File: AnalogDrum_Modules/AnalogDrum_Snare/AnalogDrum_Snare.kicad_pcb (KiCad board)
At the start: 2 copper layers, 100.3 x 160 mm, 143 parts, among them J101 Conn_01x05_Male, Q201 2N3904, Q202 2N3904, Q501 2N3904, Q502 2N3904, Q503 2N3904, SW601 SW_DPDT_x2, SW602 SW_DPDT_x2, U201 NE5532, U301 NE5532, U302 NE5532, U401 LM13700, U402 NE5532, U501 TL074, U502 LM358, U601 TL074, U701 NE5532

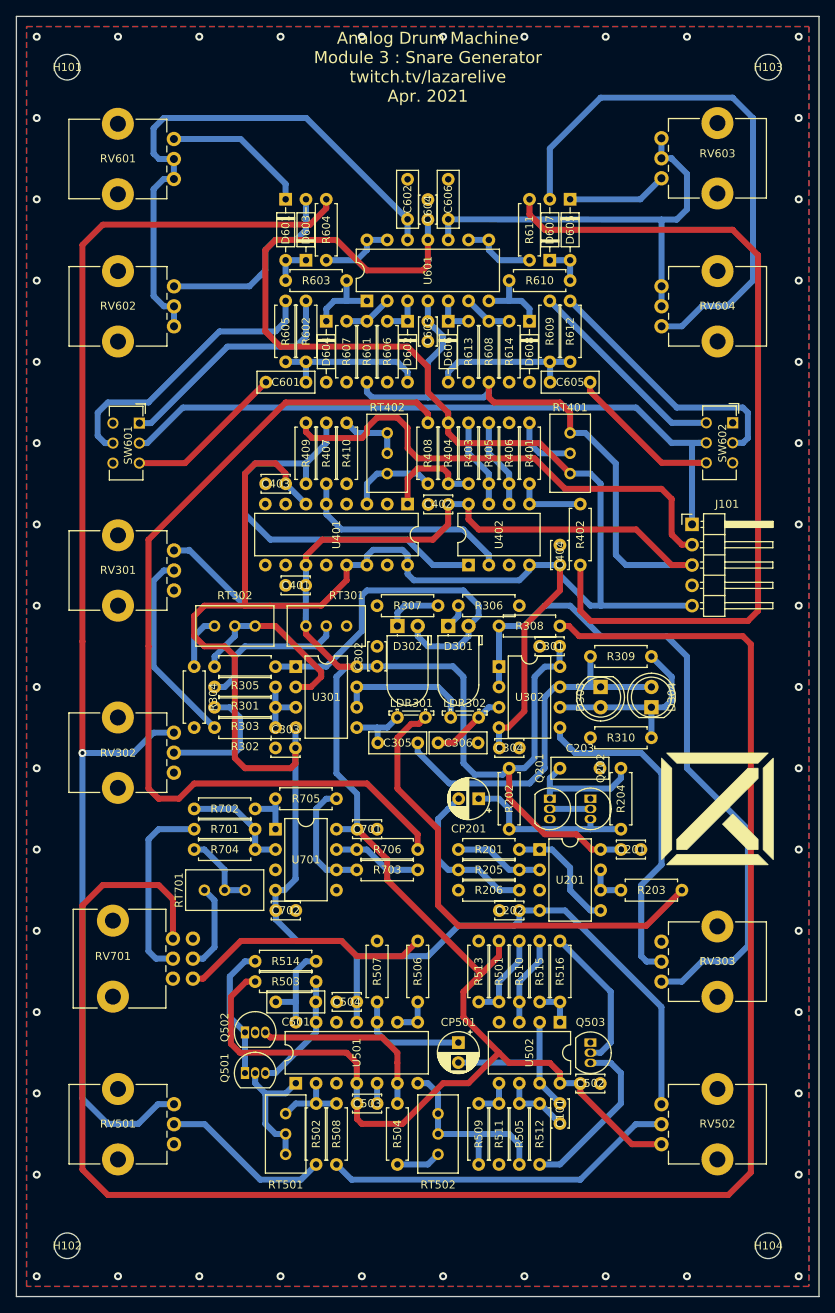
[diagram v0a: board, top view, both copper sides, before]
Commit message: Version 0.1.1
Corrections mineures :
- Vérification des potentiomètres
- Passage des connecteurs de carte e n JST
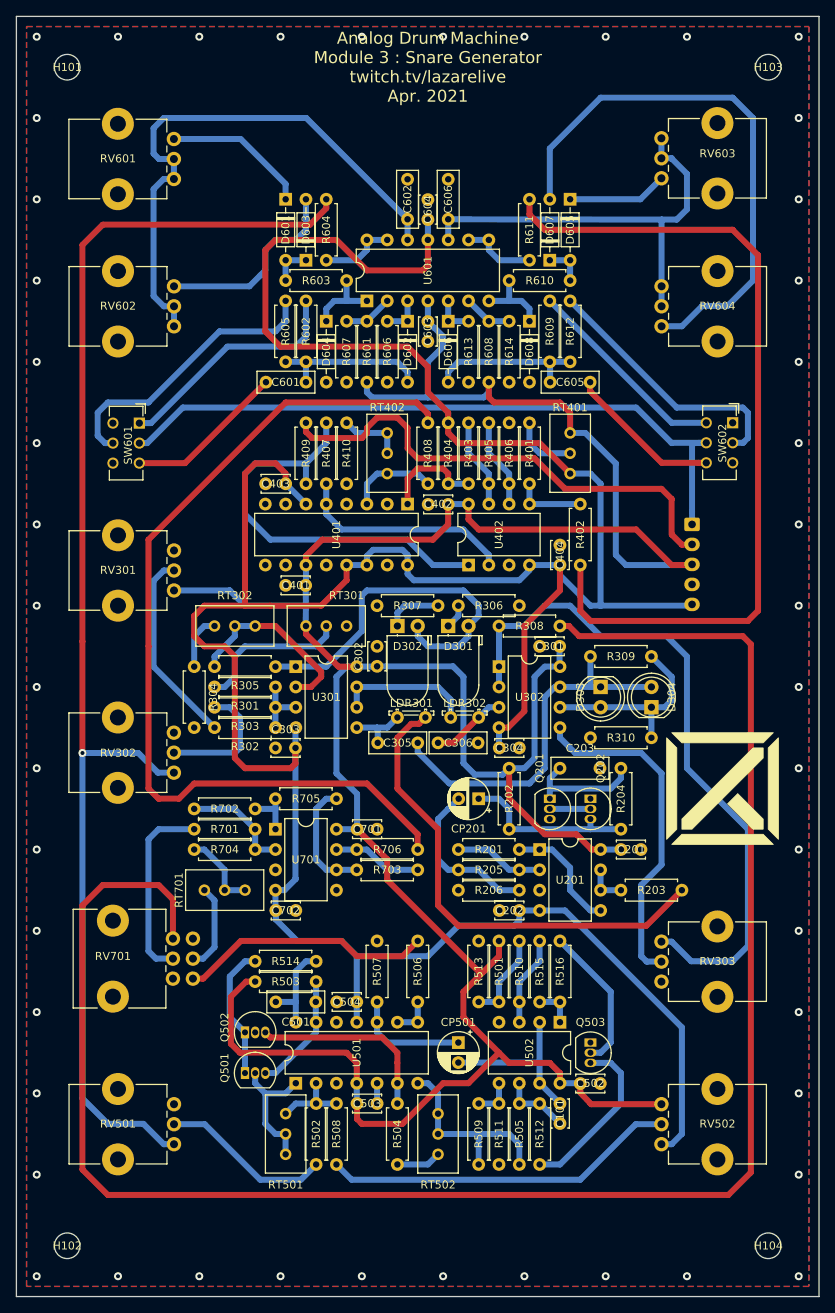
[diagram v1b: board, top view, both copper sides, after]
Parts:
- J101: footprint Connector_PinHeader_2.54mm:PinHeader_1x05_P2.54mm_Horizontal -> Connector_JST:JST_EH_B5B-EH-A_1x05_P2.50mm_Vertical; moved to B.Cu
- moved REF** 2.62 mm to (132.7, 120.7)
- turned J101 to 270 degrees
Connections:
- RV301 pad 1: +12V -> GNDA
- RV301 pad 3: GNDA -> +12V
- RV302 pad 1: /EG/EGA_OUT -> GNDA
- RV302 pad 3: GNDA -> /EG/EGA_OUT
- RV303 pad 1: Net-(R308-Pad2) -> GNDA
- RV303 pad 3: GNDA -> Net-(R308-Pad2)
- RV501 pad 1: /EG/EGA_OUT -> GNDA
- RV501 pad 3: GNDA -> /EG/EGA_OUT
- RV502 pad 1: +12V -> -12V
- RV502 pad 3: -12V -> +12V
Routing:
- net -12V: track 371.6 -> 379.5 mm
- net +12V: track 391.7 -> 387.5 mm
